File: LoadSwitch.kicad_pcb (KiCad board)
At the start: 2 copper layers, 36.6 x 26.9 mm, 20 parts, among them IC1 LTC4359, P1 CONN_01X03, P2 CONN_01X03, P3 CONN_01X02, P4 CONN_01X02, Q1 FDMS86101, Q2 FDMS86101

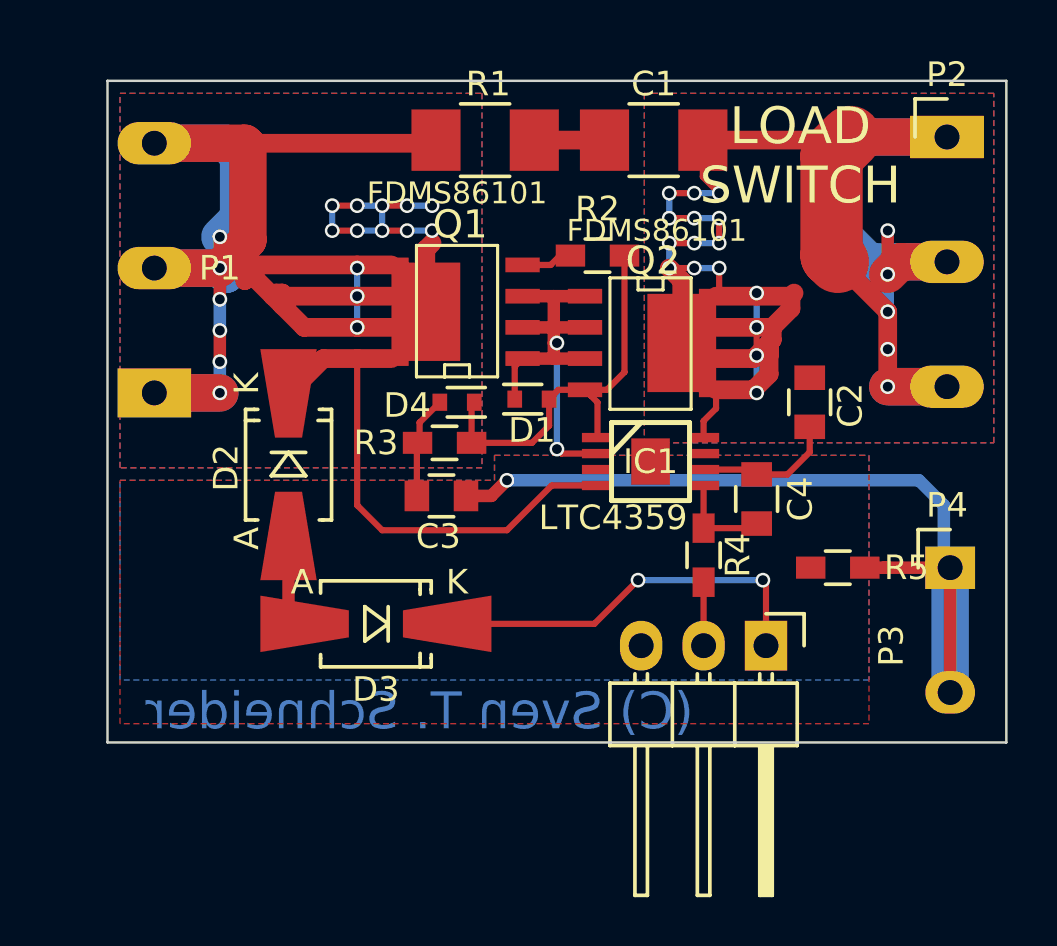
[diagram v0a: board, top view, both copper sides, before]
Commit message: Korrekte Ansteuerung des SHDN pins
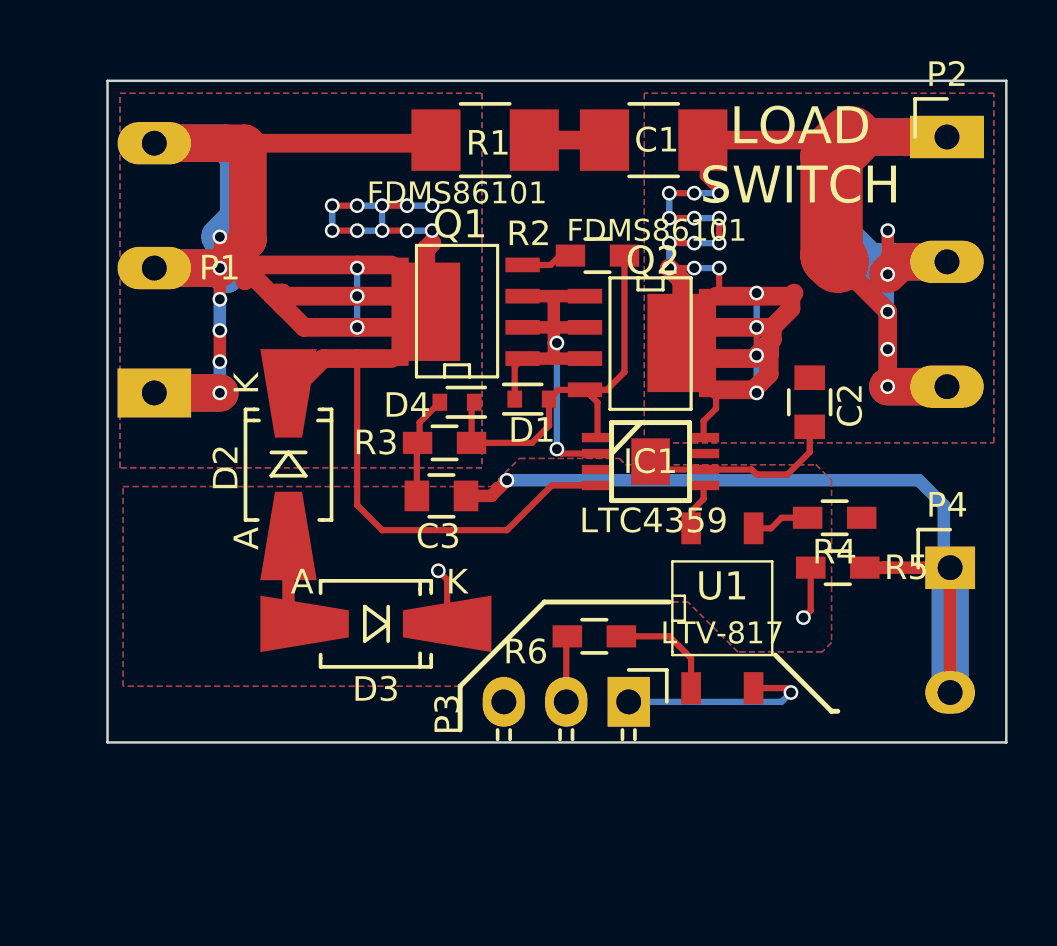
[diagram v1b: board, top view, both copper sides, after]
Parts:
- removed C4: 10n, Capacitors_SMD:C_0805
- added R6: 1k, Resistors_SMD:R_0603_HandSoldering, F.Cu at (167.6, 83.1)
- added U1: LTV-817, Toni:SO-4, F.Cu at (172.8, 81.9)
- R4: value 100k -> 1k
- moved P3 6.04 mm to (169.0, 85.7)
- moved R4 5.55 mm to (177.4, 78.2), turned to 180 degrees
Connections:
- IC1 pad 5: Net-(C4-Pad1) -> Net-(IC1-Pad5)
- IC1 pad 9: (no net) -> Vss
- P3 pad 1: Vss -> Net-(P3-Pad1)
- R4 pad 1: Net-(C4-Pad1) -> GND
- R4 pad 2: Net-(P3-Pad2) -> Net-(R4-Pad2)
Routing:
- net Vss: track 22.1 -> 12.6 mm
- net Net-(P3-Pad1): track 0.00 -> 8.36 mm, vias 0 -> 1
- net Net-(R6-Pad2): track 0.00 -> 4.42 mm
- net Net-(C4-Pad1): track 3.97 -> 0.00 mm
- net Net-(R4-Pad2): track 0.00 -> 2.38 mm
- net Net-(IC1-Pad5): track 0.00 -> 1.95 mm
